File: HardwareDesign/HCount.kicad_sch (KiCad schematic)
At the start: 8 parts, among them U102 GAL22V10, U103 74ACT163, U104 74ACT163, U105 74ACT163

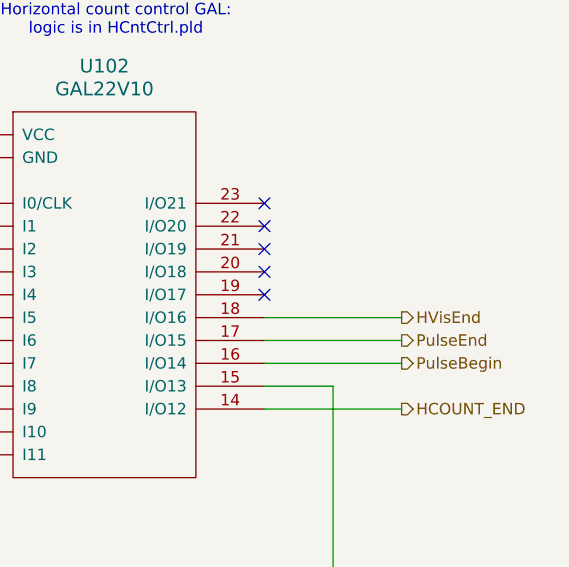
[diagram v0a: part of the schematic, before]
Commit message: use net labels rather than wires on main page
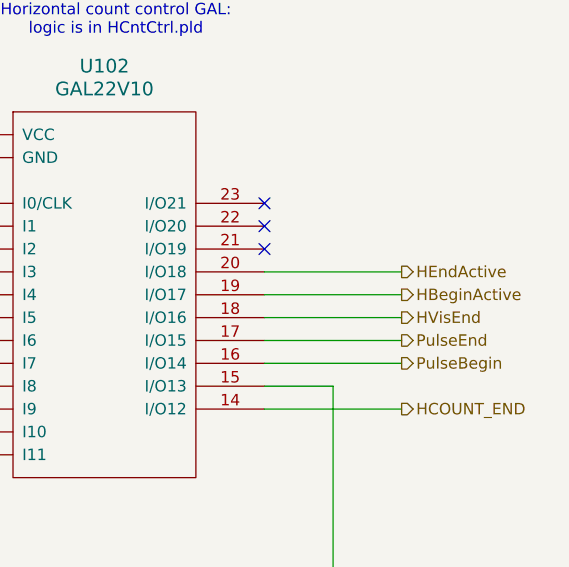
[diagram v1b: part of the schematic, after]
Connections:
- net HBeginActive: now reaches U102.19 (I/O17)
- net HEndActive: now reaches U102.20 (I/O18)
- no-connect marks 5 -> 3
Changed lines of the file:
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@@
-	)
-	(no_connect
-		(at 234.95 110.49)
 	)
 	(no_connect
@@
 		(at 234.95 107.95)
 	)
-	(no_connect
-		(at 234.95 113.03)
-	)
 	(bus_entry
 		(at 181.61 44.45)
@@
 	(wire
 		(pts
+			(xy 234.95 110.49) (xy 250.19 110.49)
+		)
+		(stroke
+			(width 0)
+			(type default)
+		)
+	)
+	(wire
+		(pts
 			(xy 35.56 151.13) (xy 35.56 121.92)
 		)
@@
 		(pts
 			(xy 63.5 96.52) (xy 71.12 96.52)
+		)
+		(stroke
+			(width 0)
+			(type default)
+		)
+	)
+	(wire
+		(pts
+			(xy 234.95 113.03) (xy 250.19 113.03)
 		)
 		(stroke
@@
 		)
 	)
+	(hierarchical_label "HEndActive"
+		(shape output)
+		(at 250.19 110.49 0)
+		(fields_autoplaced yes)
+		(effects
+			(font
+				(size 1.27 1.27)
+			)
+			(justify left)
+		)
+	)
 	(hierarchical_label "HC0"
 		(shape output)
@@
 		(fields_autoplaced yes)
 		(effects
+			(font
+				(size 1.27 1.27)
+			)
+			(justify left)
+		)
+	)
+	(hierarchical_label "HBeginActive"
+		(shape output)
+		(at 250.19 113.03 0)
+		(fields_autoplaced yes)
+		(effects

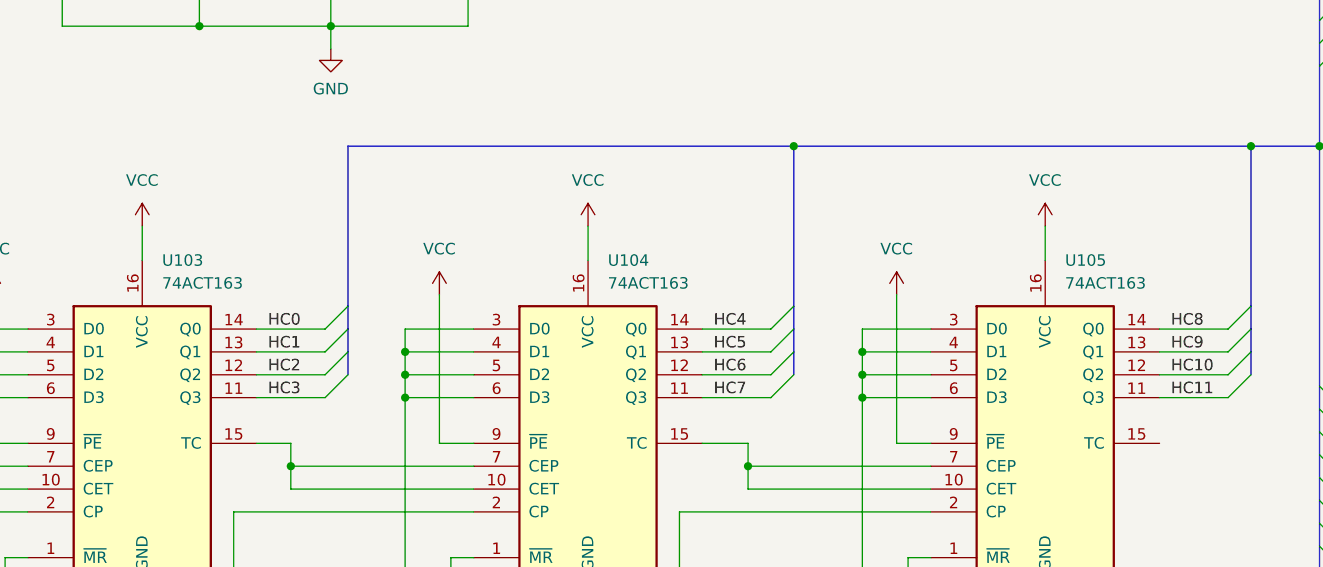
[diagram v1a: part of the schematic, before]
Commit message: use 74ALS163 rather than 74ACT163
The prototype did not work reliably with 74ACT163 counters,
but did work correctly with 74ALS163 counters.
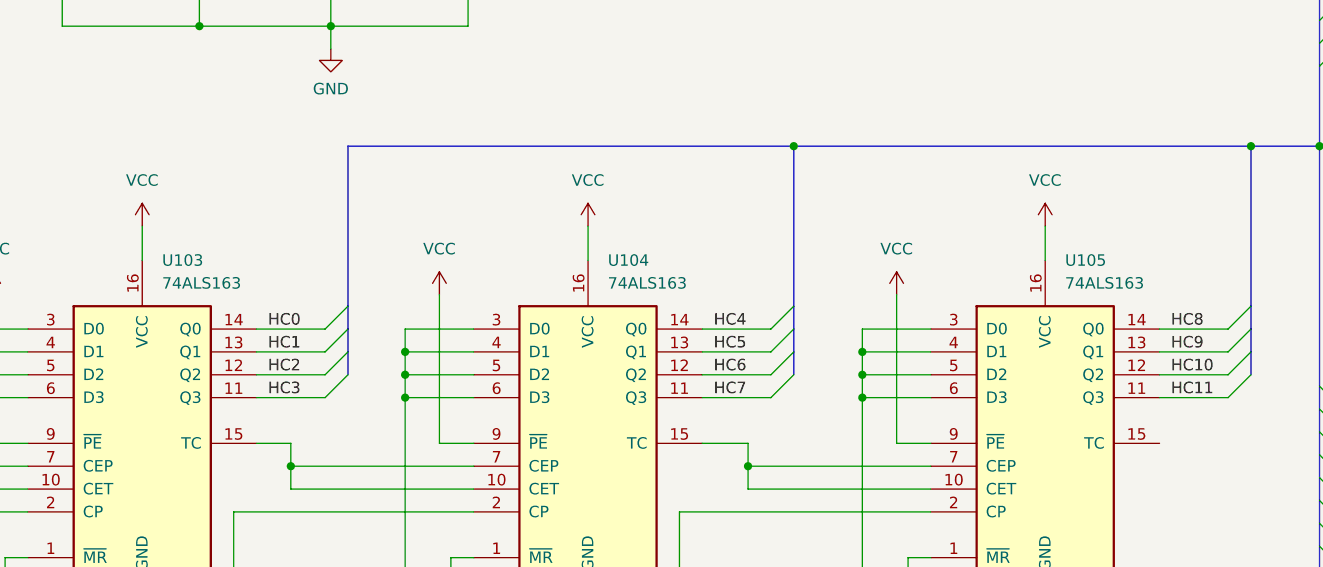
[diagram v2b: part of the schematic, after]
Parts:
- U103, U104, U105: value 74ACT163 -> 74ALS163
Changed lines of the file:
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@@
 			)
 		)
-		(property "Value" "74ACT163"
+		(property "Value" "74ALS163"
 			(at 52.9941 91.44 0)
 			(effects
@@
 			)
 		)
-		(property "Value" "74ACT163"
+		(property "Value" "74ALS163"
 			(at 153.3241 91.44 0)
 			(effects
@@
 			)
 		)
-		(property "Value" "74ACT163"
+		(property "Value" "74ALS163"
 			(at 102.5241 91.44 0)
 			(effects

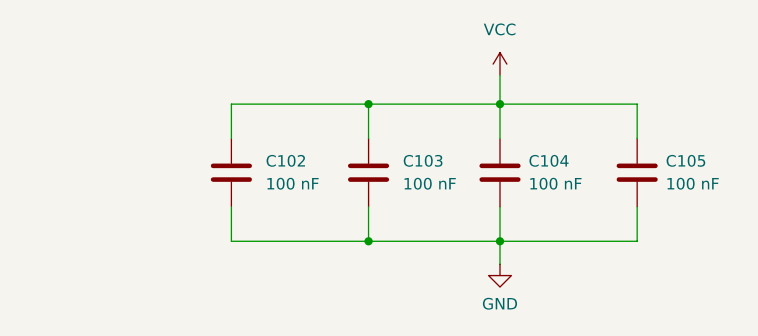
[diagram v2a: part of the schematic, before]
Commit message: label decoupling caps
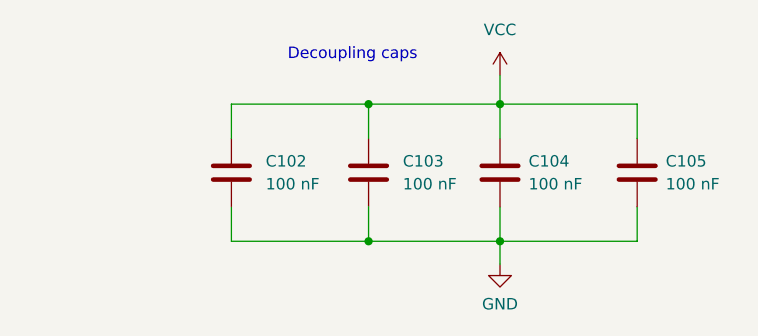
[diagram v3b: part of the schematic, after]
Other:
- note added: "Decoupling caps"
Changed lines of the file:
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@@
+		)
+	)
+	(text "Decoupling caps"
+		(exclude_from_sim no)
+		(at 55.372 42.164 0)
+		(effects
+			(font
+				(size 1.27 1.27)
+			)
 		)
 	)
